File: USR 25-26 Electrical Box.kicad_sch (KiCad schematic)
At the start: 1 part, among them J1 MCU_host

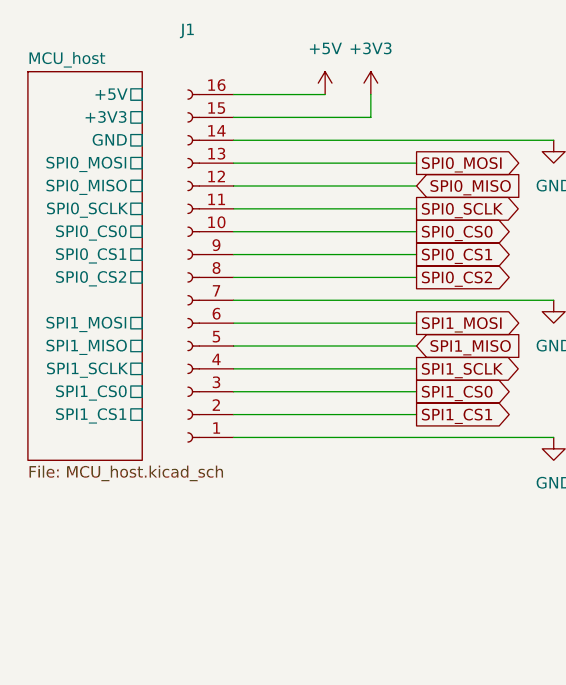
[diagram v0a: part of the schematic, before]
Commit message: Added indicator LEDs for power and 4 configurable status LEDs to the MCU host board. Waiting on a decision regarding placement of 3-to-8 and 2-to-4 decoder chips.
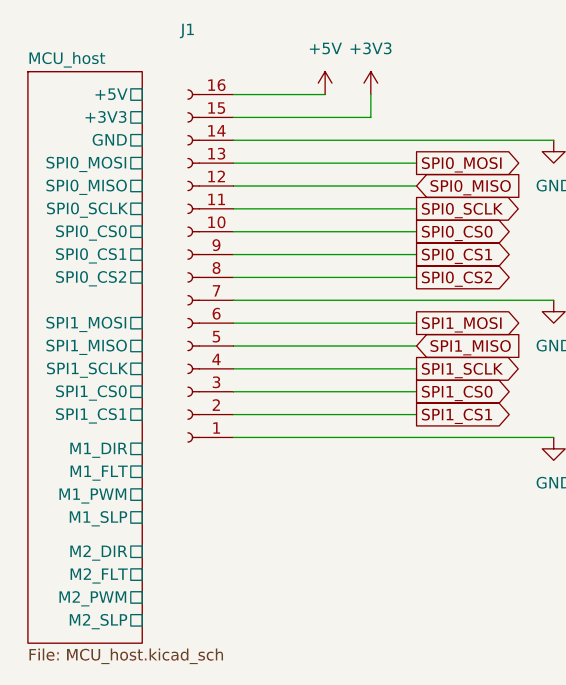
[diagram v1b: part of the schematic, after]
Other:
- sheet MCU_host ports: added M1_DIR, M1_FLT, M1_PWM, M1_SLP, M2_DIR, M2_FLT, M2_PWM, M2_SLP; removed none
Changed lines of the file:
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@@
 	(sheet
 		(at 30.48 24.13)
-		(size 12.7 43.18)
+		(size 12.7 63.5)
 		(exclude_from_sim no)
 		(in_bom yes)
@@
 		)
 		(property "Sheetfile" "MCU_host.kicad_sch"
-			(at 30.48 67.8946 0)
+			(at 30.48 88.2146 0)
 			(effects
 				(font
@@
 			(effects
 				(font
+					(size 1.27 1.27)
+				)
+				(justify right)
+			)
+		)
+		(pin "M1_DIR" passive
+			(at 43.18 66.04 0)
+			(effects
+				(font
+					(size 1.27 1.27)
+				)
+				(justify right)
+			)
+		)
+		(pin "M1_FLT" passive
+			(at 43.18 68.58 0)
+			(effects
+				(font
+					(size 1.27 1.27)
+				)
+				(justify right)
+			)
+		)
+		(pin "M1_PWM" passive
+			(at 43.18 71.12 0)
+			(effects
+				(font
+					(size 1.27 1.27)
+				)
+				(justify right)
+			)
+		)
+		(pin "M1_SLP" passive
+			(at 43.18 73.66 0)
+			(effects
+				(font
+					(size 1.27 1.27)
+				)
+				(justify right)
+			)
+		)
+		(pin "M2_DIR" passive
+			(at 43.18 77.47 0)
+			(effects
+				(font
+					(size 1.27 1.27)
+				)
+				(justify right)
+			)
+		)
+		(pin "M2_FLT" passive
+			(at 43.18 80.01 0)
+			(effects
+				(font
+					(size 1.27 1.27)
+				)
+				(justify right)
+			)
+		)
+		(pin "M2_PWM" passive
+			(at 43.18 82.55 0)
+			(effects
+				(font
+					(size 1.27 1.27)
+				)
+				(justify right)
+			)
+		)
+		(pin "M2_SLP" passive
+			(at 43.18 85.09 0)
+			(effects
+				(font

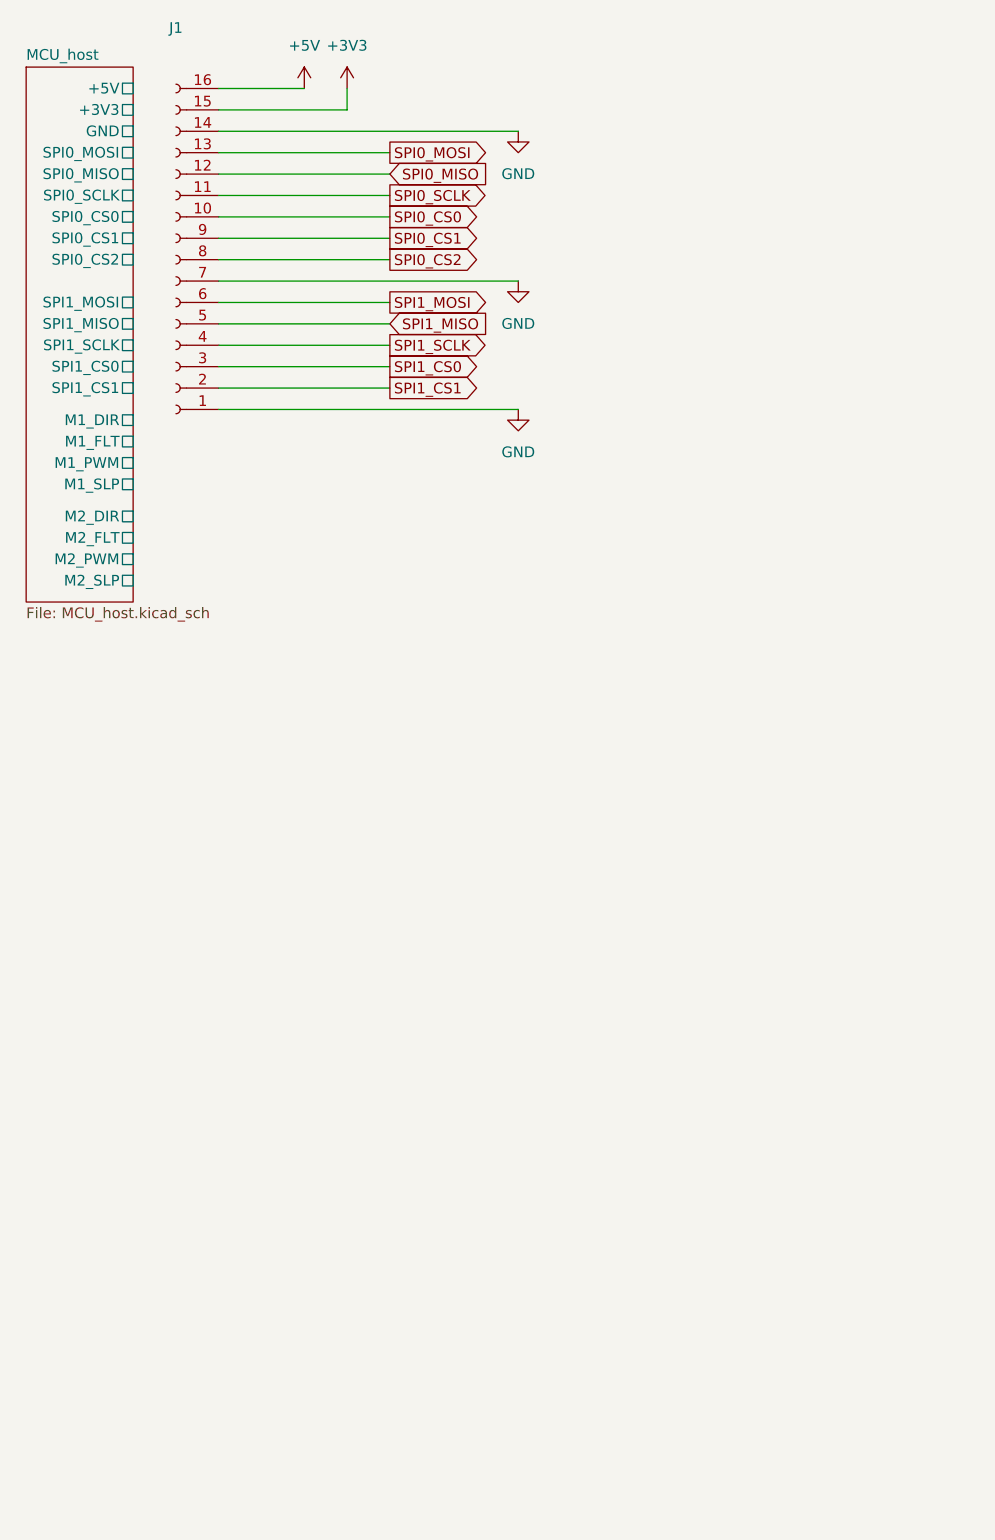
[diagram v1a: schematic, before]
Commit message: Staged initial slot connections for backplane. May need to separate individual boards into separate projects.
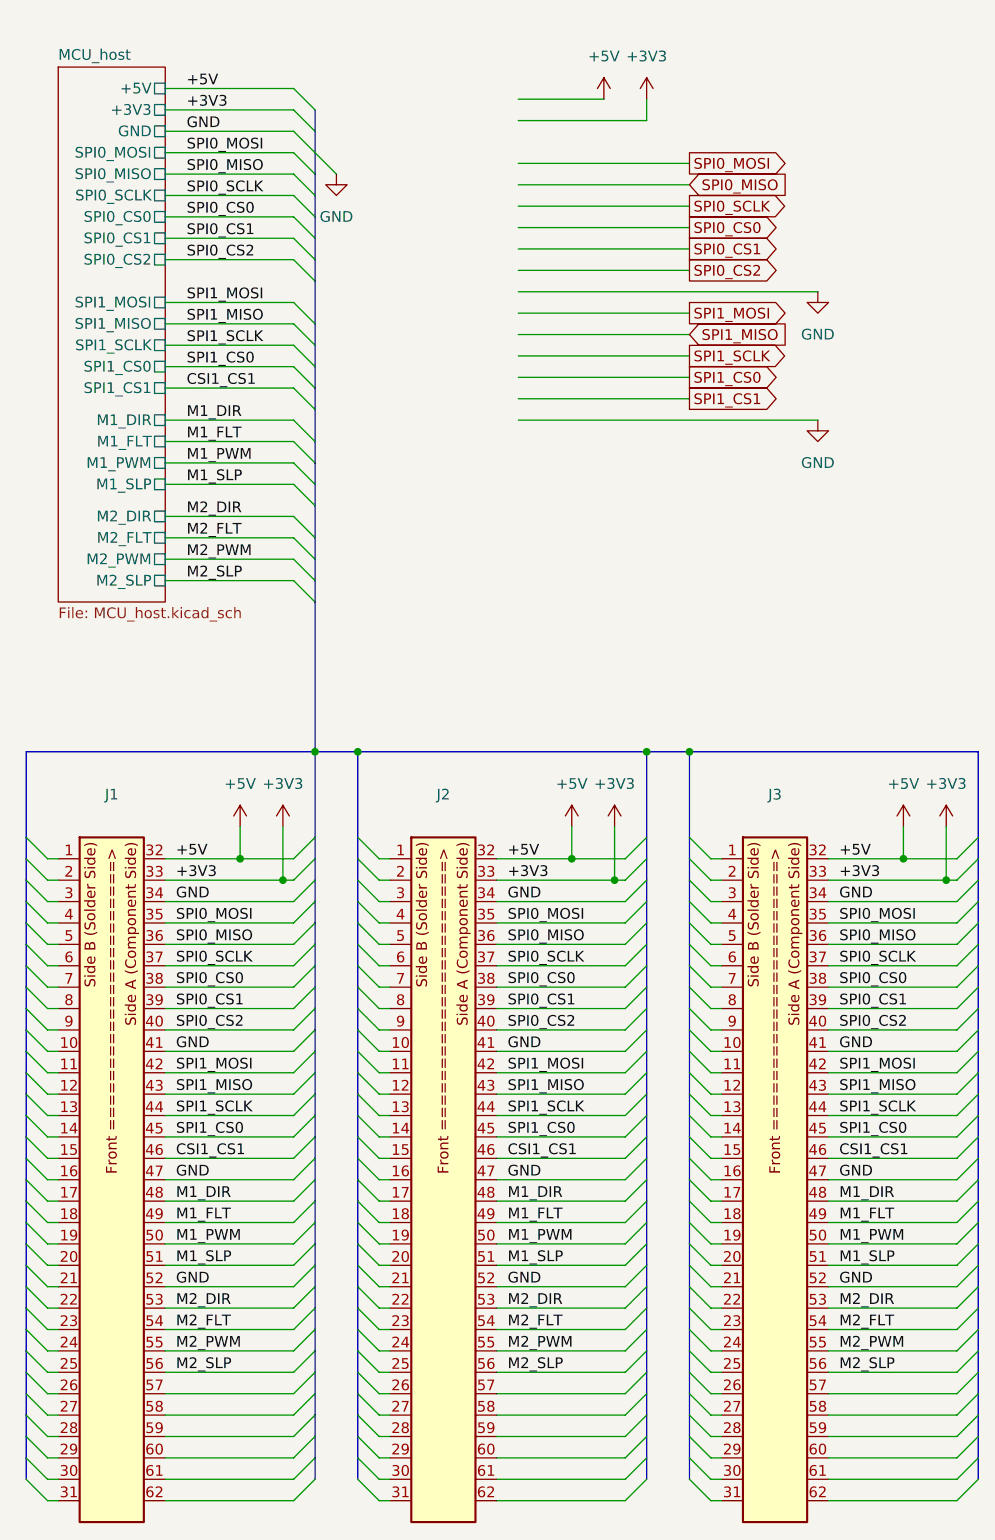
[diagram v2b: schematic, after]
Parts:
- removed J1: MCU_host, symbol Connector:Conn_01x16_Socket
- added J1, J2, J3: ~, USR:TE_7-5530843-0, symbol USR:62_PIN_EDGE_ISA
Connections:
- net +3V3: now also J1.33, J2.33, J3.33
- net +5V: now also J1.32, J2.32, J3.32
- net GND: now also J1.34, J1.41, J1.47, J1.52, J2.34, J2.41, J2.47, J2.52, J3.34, J3.41, J3.47, J3.52
- net SPI0_CS0: now also J1.38, J2.38, J3.38
- net SPI0_CS1: now also J1.39, J2.39, J3.39
- net SPI0_CS2: now also J1.40, J2.40, J3.40
- net SPI0_MISO: now also J1.36, J2.36, J3.36
- net SPI0_MOSI: now also J1.35, J2.35, J3.35
- net SPI0_SCLK: now also J1.37, J2.37, J3.37
- net SPI1_CS0: now also J1.45, J2.45, J3.45
- net SPI1_MISO: now also J1.43, J2.43, J3.43
- net SPI1_MOSI: now also J1.42, J2.42, J3.42
- net SPI1_SCLK: now also J1.44, J2.44, J3.44
- new net CSI1_CS1: J1.46, J2.46, J3.46
- new net M1_DIR: J1.48, J2.48, J3.48
- new net M1_FLT: J1.49, J2.49, J3.49
- new net M1_PWM: J1.50, J2.50, J3.50
- new net M1_SLP: J1.51, J2.51, J3.51
- new net M2_DIR: J1.53, J2.53, J3.53
- new net M2_FLT: J1.54, J2.54, J3.54
- new net M2_PWM: J1.55, J2.55, J3.55
- new net M2_SLP: J1.56, J2.56, J3.56
